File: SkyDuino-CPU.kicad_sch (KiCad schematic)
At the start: 0 parts

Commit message: WIP CPU
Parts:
- added C12, C13, C14, C15, C17: 100nF, Capacitor_SMD:C_0805_2012Metric_Pad1.18x1.45mm_HandSolder, symbol Device:C
- added C16: 2.2µF, Capacitor_SMD:C_1210_3225Metric_Pad1.33x2.70mm_HandSolder, symbol Device:C_Small
- added C18, C19: 2.2µF, Capacitor_SMD:C_1210_3225Metric_Pad1.33x2.70mm_HandSolder, symbol Device:C
- added L2: L_Ferrite_Small, symbol Device:L_Ferrite_Small
- added U6: STM32F411RET6, Package_QFP:LQFP-64_10x10mm_P0.5mm, symbol MCU_ST_STM32F4:STM32F411RETx
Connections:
- new net: C17.1, L2.2, U6.13 (VDDA)
- new net: L2.1, U6.19 (VDD), U6.32 (VDD), U6.48 (VDD), U6.64 (VDD)
- new net: C16.1, U6.30 (VCAP1)
- new net +3V3: C12.1, C13.1, C14.1, C15.1, C18.1, C19.1
- new net GND: C12.2, C13.2, C14.2, C15.2, C16.2, C17.2, C18.2, C19.2, U6.12 (VSSA), U6.18 (VSS), U6.31 (VSS), U6.47 (VSS), U6.63 (VSS)

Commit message: WIP CPU boot switches
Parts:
- added R8, R9: 10kΩ, Resistor_SMD:R_0805_2012Metric, symbol Device:R
- added SW1: BOOT, symbol Switch:SW_Push
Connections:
- net +3V3: now also L2.1, U6.19 (VDD), U6.32 (VDD), U6.48 (VDD), U6.64 (VDD), SW1.2
- net GND: now also R8.2, R9.2
- net PB2: now reaches U6.28 (PB2)
- net PB2: now also R8.1
- net BOOT0: now reaches U6.60 (BOOT0)
- net BOOT0: now also R9.1, SW1.1

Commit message: Add Oscillators
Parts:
- added C20, C21: 7.5pF, Capacitor_SMD:C_0805_2012Metric_Pad1.18x1.45mm_HandSolder, symbol Device:C_Small
- added C22, C23: 11pF, Capacitor_SMD:C_0805_2012Metric_Pad1.18x1.45mm_HandSolder, symbol Device:C_Small
- added J8: DBG, Connector_PinHeader_2.54mm:PinHeader_1x04_P2.54mm_Vertical, symbol Connector_Generic:Conn_01x04
- added U7: 25MHz, Oscillator:Oscillator_SMD_Kyocera_KC2520Z-4Pin_2.5x2.0mm, symbol Oscillator:KC2520Z
- added Y1: 32.768kHz, symbol Device:Crystal_GND23
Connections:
- net +3V3: now also J8.1 (Pin_1), U7.4 (VCC)
- net GND: now also C20.1, C21.1, C22.2, C23.2, J8.4 (Pin_4), U7.2 (GND), Y1.2, Y1.3
- net at U6.3 (PC14): now also C20.2, Y1.4
- net at U6.4 (PC15): now also C21.2, Y1.1
- net SWDIO: now reaches U6.46 (PA13)
- net SWDIO: now also J8.2 (Pin_2)
- net SWCLK: now reaches U6.49 (PA14)
- net SWCLK: now also J8.3 (Pin_3)
- net at U6.5 (PH0): now also C22.1, U7.1 (INH)
- net at U6.6 (PH1): now also C23.1, U7.3 (CLK)

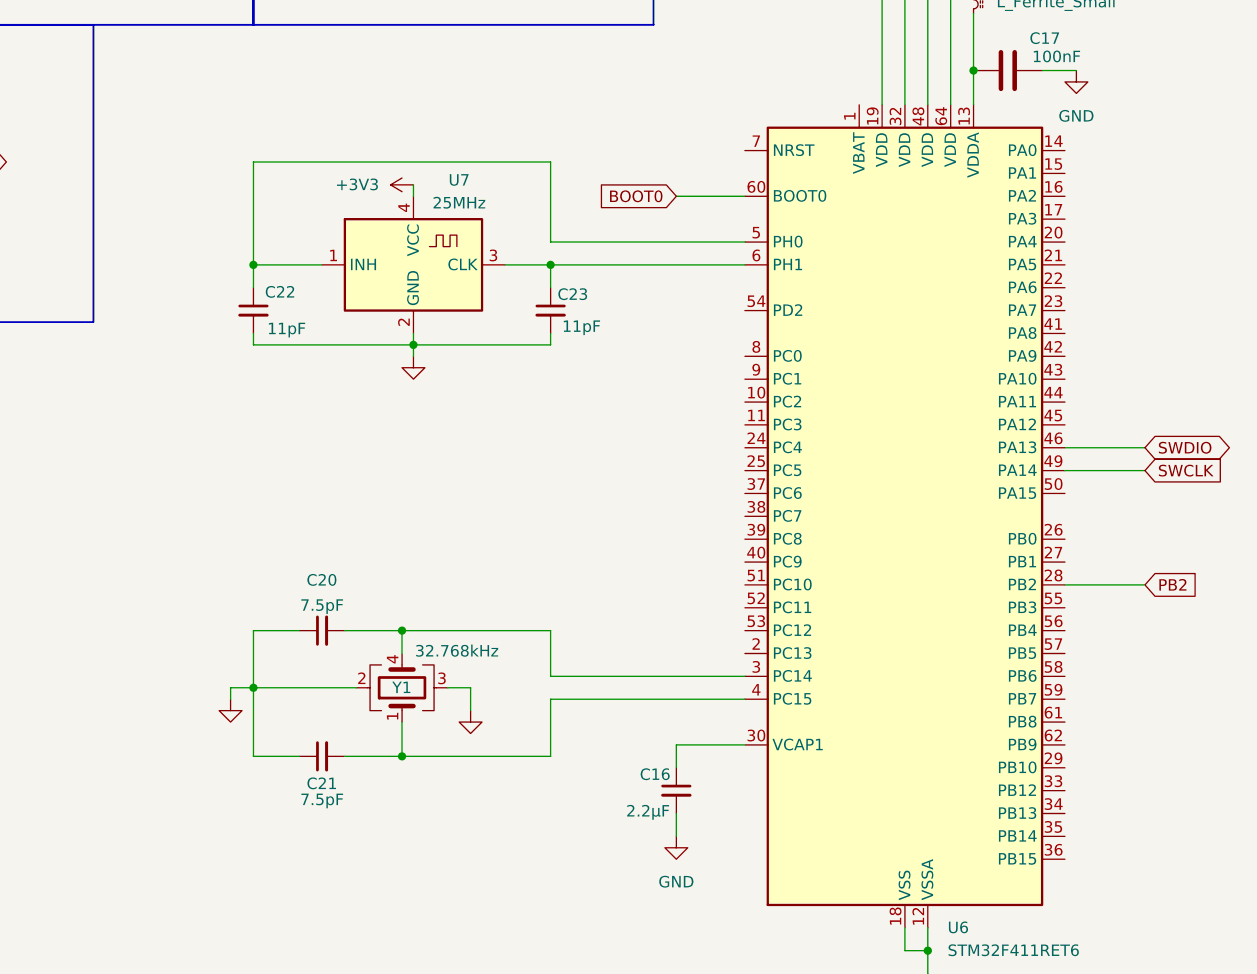
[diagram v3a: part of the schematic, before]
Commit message: Rough in on MCU control connections
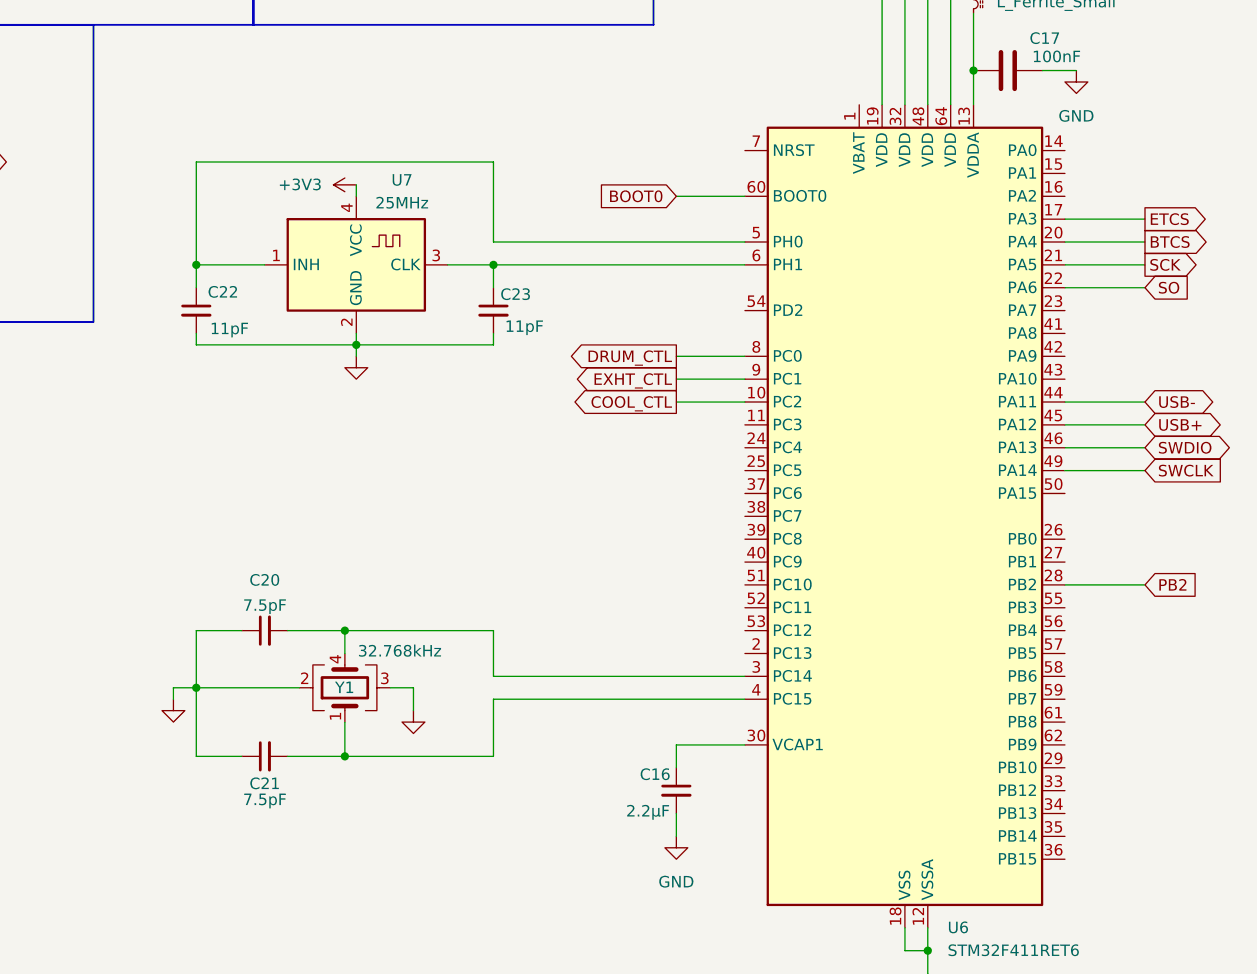
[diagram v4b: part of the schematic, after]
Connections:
- net COOL_CTL: now reaches U6.10 (PC2)
- net ETCS: now reaches U6.17 (PA3)
- net BTCS: now reaches U6.20 (PA4)
- net SCK: now reaches U6.21 (PA5)
- net SO: now reaches U6.22 (PA6)
- net USB-: now reaches U6.44 (PA11)
- net USB+: now reaches U6.45 (PA12)
- net DRUM_CTL: now reaches U6.8 (PC0)
- net EXHT_CTL: now reaches U6.9 (PC1)
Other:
- moved on the sheet: C20, C21, C22, C23, U7, Y1

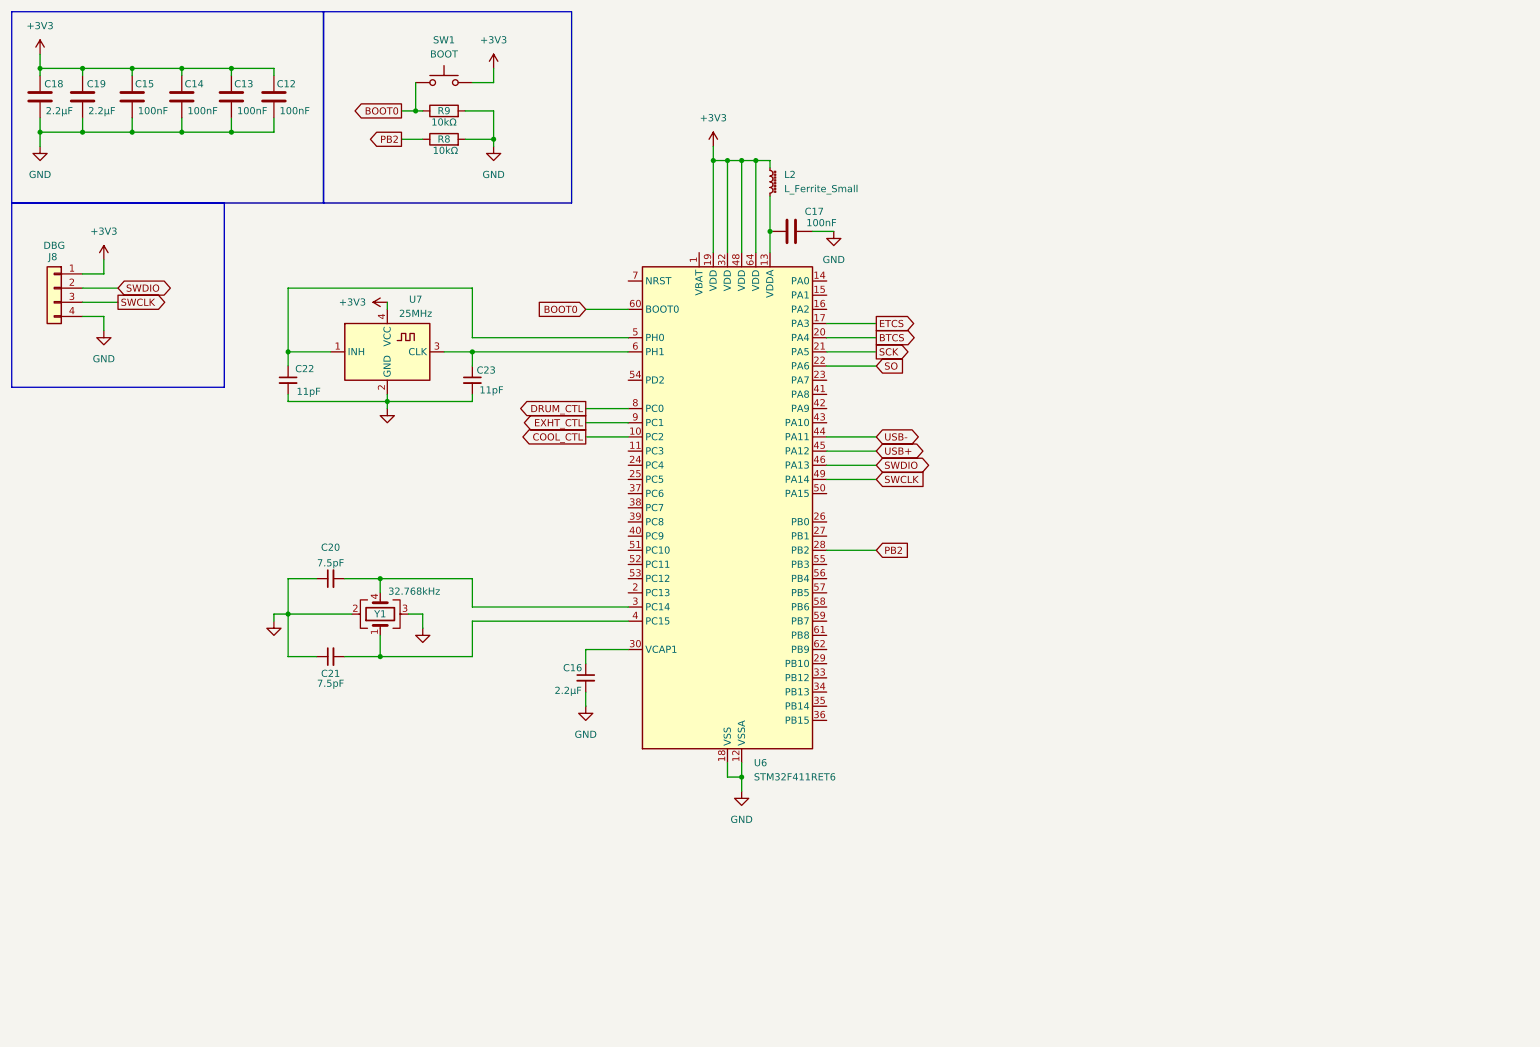
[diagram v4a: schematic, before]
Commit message: Add USB-C connector
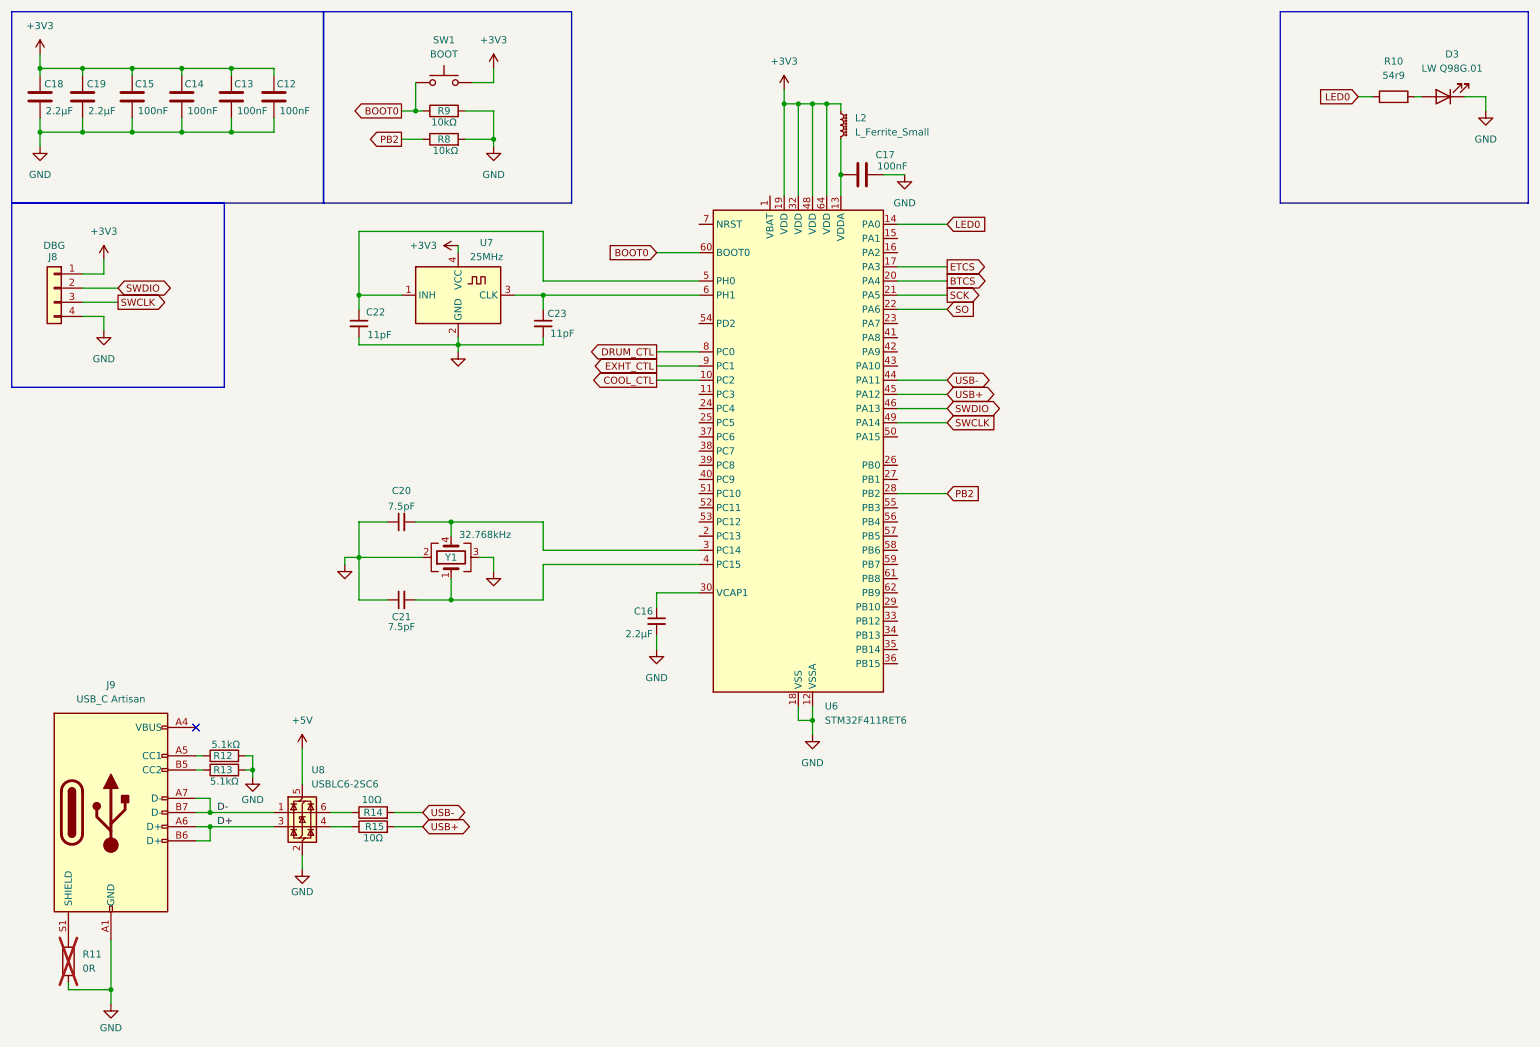
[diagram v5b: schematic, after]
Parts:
- added D3: LW Q98G.01, LED_SMD:LED_0805_2012Metric_Pad1.15x1.40mm_HandSolder, symbol Device:LED
- added J9: USB_C Artisan, symbol Connector:USB_C_Receptacle_USB2.0_14P
- added R10: 54r9, Resistor_SMD:R_0805_2012Metric_Pad1.20x1.40mm_HandSolder, symbol Device:R
- added R11: 0R, Resistor_SMD:R_0805_2012Metric_Pad1.20x1.40mm_HandSolder, symbol Device:R
- added R12, R13: 5.1kΩ, Resistor_SMD:R_0805_2012Metric_Pad1.20x1.40mm_HandSolder, symbol Device:R
- added R14, R15: 10Ω, Resistor_SMD:R_0805_2012Metric_Pad1.20x1.40mm_HandSolder, symbol Device:R
- added U8: USBLC6-2SC6, Package_TO_SOT_SMD:SOT-23-6, symbol Power_Protection:USBLC6-2SC6
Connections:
- net GND: now also D3.1 (K), J9.A1 (GND), J9.A12 (GND), J9.B1 (GND), J9.B12 (GND), R11.2, R12.2, R13.2, U8.2 (GND)
- net USB+: now also R15.2
- net USB-: now also R14.2
- net LED0: now reaches U6.14 (PA0)
- net LED0: now also R10.1
- new net: R14.1, U8.6 (I/O1)
- new net: R15.1, U8.4 (I/O2)
- new net: D3.2 (A), R10.2
- new net: J9.A4 (VBUS), J9.A9 (VBUS), J9.B4 (VBUS), J9.B9 (VBUS)
- new net: J9.A5 (CC1), R12.1
- new net: J9.B5 (CC2), R13.1
- new net: J9.S1 (SHIELD), R11.1
- new net +5V: U8.5 (VBUS)
- new net D+: J9.A6 (D+), J9.B6 (D+), U8.3 (I/O2)
- new net D-: J9.A7 (D-), J9.B7 (D-), U8.1 (I/O1)
- no-connect marks 0 -> 1
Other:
- moved on the sheet: C16, C17, C20, C21, C22, C23, L2, U6, U7, Y1

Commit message: Add Footprint for USB-C receptacle
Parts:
- J9: footprint (none) -> Connectors:USB_C_Receptacle_Molex_Upright
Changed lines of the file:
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@@
 			)
 		)
-		(property "Footprint" ""
+		(property "Footprint" "Connectors:USB_C_Receptacle_Molex_Upright"
 			(at 34.29 157.48 0)
 			(effects

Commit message: Update footprint for the boot button
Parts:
- SW1: footprint (none) -> Button_Switch_THT:SW_PUSH_6mm_H4.3mm
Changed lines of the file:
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@@
 			)
 		)
-		(property "Footprint" ""
+		(property "Footprint" "Button_Switch_THT:SW_PUSH_6mm_H4.3mm"
 			(at 90.17 21.59 0)
 			(effects

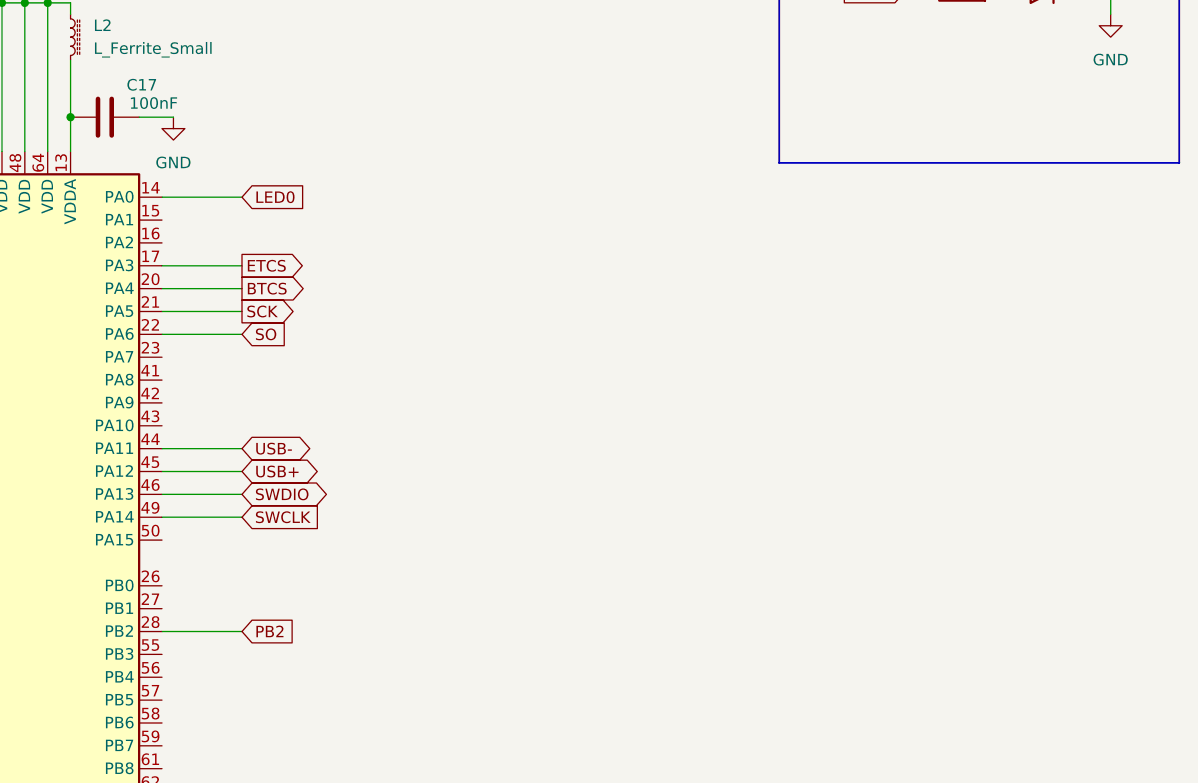
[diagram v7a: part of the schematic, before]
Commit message: Add USB-A for the remote
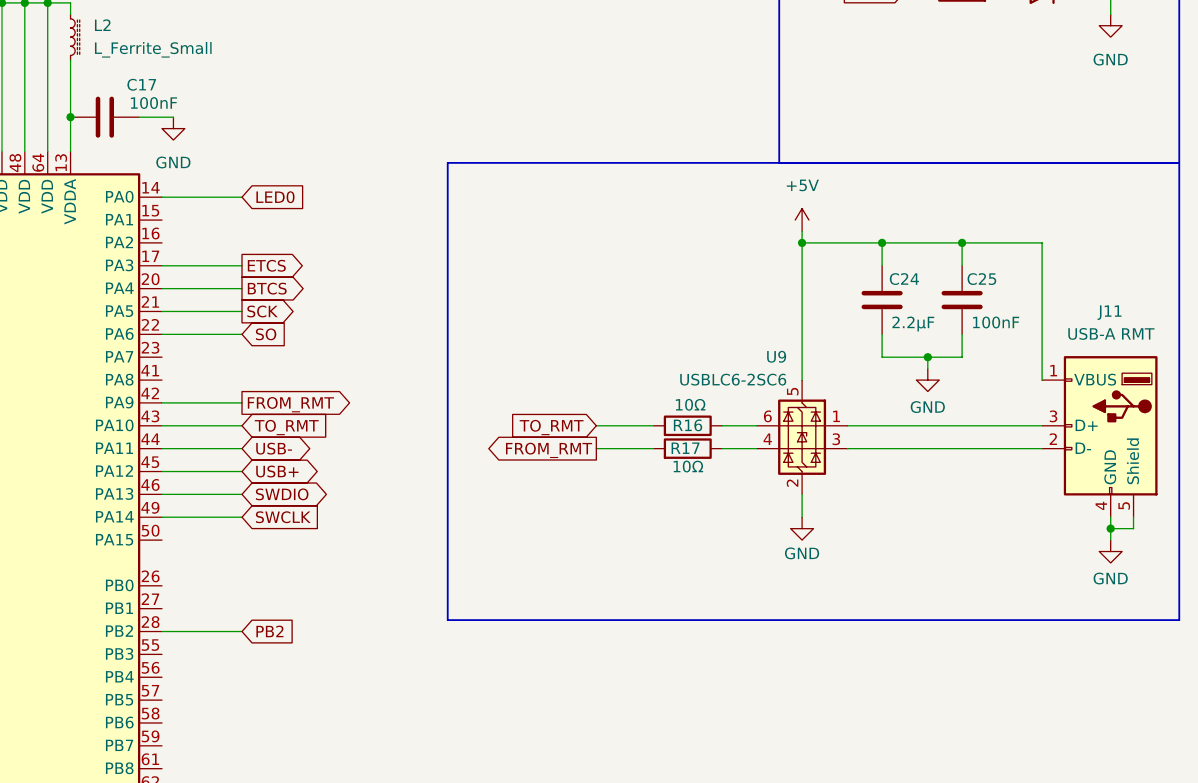
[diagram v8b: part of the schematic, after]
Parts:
- added C24: 2.2µF, Capacitor_SMD:C_1210_3225Metric_Pad1.33x2.70mm_HandSolder, symbol Device:C
- added C25: 100nF, Capacitor_SMD:C_0805_2012Metric_Pad1.18x1.45mm_HandSolder, symbol Device:C
- added J11: USB-A RMT, Connector_USB:USB_A_Molex_67643_Horizontal, symbol Connector:USB_A
- added R16, R17: 10Ω, Resistor_SMD:R_0805_2012Metric_Pad1.20x1.40mm_HandSolder, symbol Device:R
- added U9: USBLC6-2SC6, Package_TO_SOT_SMD:SOT-23-6, symbol Power_Protection:USBLC6-2SC6
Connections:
- net +5V: now also C24.1, C25.1, J11.1 (VBUS), U9.5 (VBUS)
- net GND: now also C24.2, C25.2, J11.4 (GND), J11.5 (Shield), U9.2 (GND)
- net FROM_RMT: now reaches U6.42 (PA9)
- net FROM_RMT: now also R17.2
- net TO_RMT: now reaches U6.43 (PA10)
- net TO_RMT: now also R16.2
- new net: R17.1, U9.4 (I/O2)
- new net: J11.2 (D-), U9.3 (I/O2)
- new net: J11.3 (D+), U9.1 (I/O1)
- new net: R16.1, U9.6 (I/O1)
